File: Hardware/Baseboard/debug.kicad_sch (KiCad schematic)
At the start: 1 part, among them J1 Conn_02x06_Odd_Even

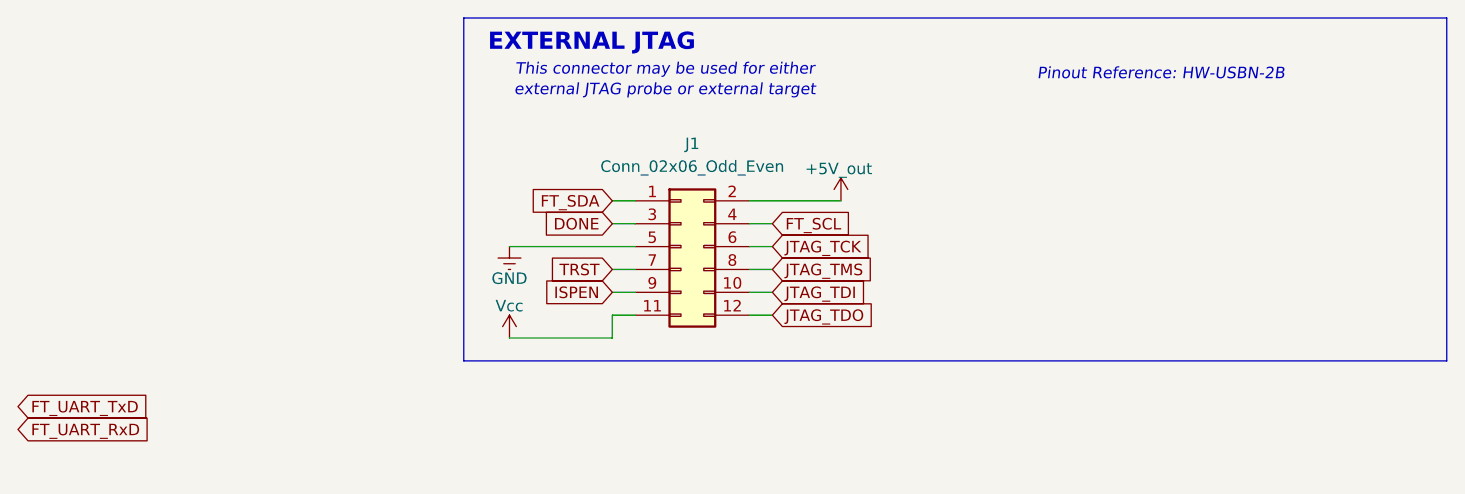
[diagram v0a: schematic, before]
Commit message: M.2 connector added
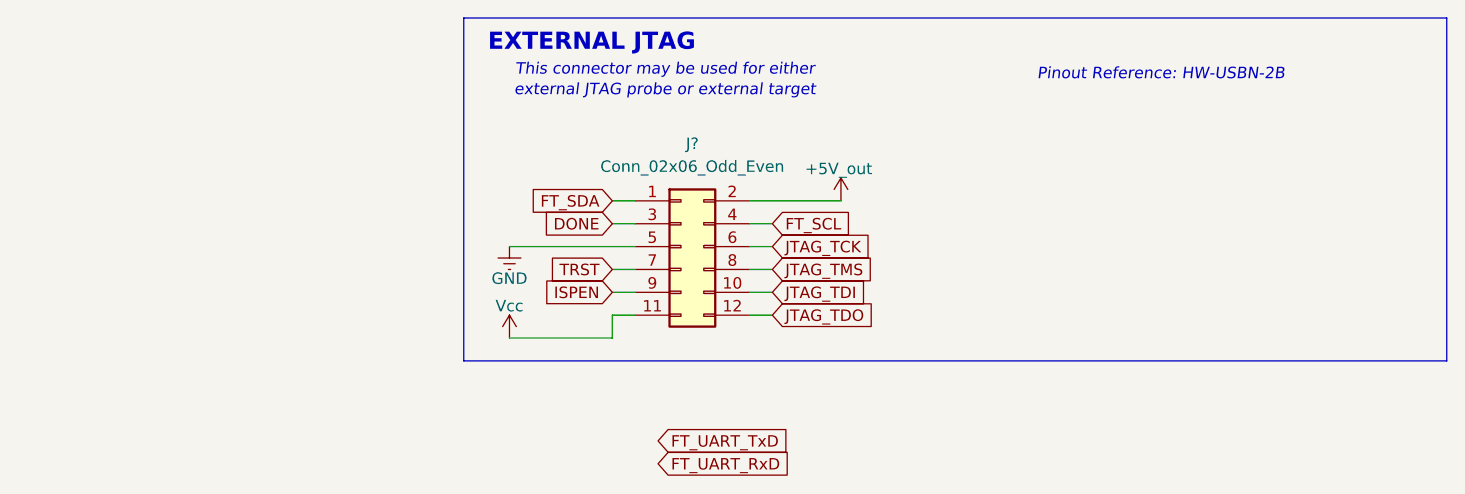
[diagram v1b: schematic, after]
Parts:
- renumbered J1 to J?
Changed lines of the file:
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@@
 	(global_label "FT_UART_RxD"
 		(shape input)
-		(at 71.12 72.39 0)
-		(fields_autoplaced yes)
-		(effects
-			(font
-				(size 1.27 1.27)
-			)
-			(justify left)
-		)
-		(property "Intersheetrefs" "${INTERSHEET_REFS}"
-			(at 86.3214 72.39 0)
+		(at 142.24 76.2 0)
+		(fields_autoplaced yes)
+		(effects
+			(font
+				(size 1.27 1.27)
+			)
+			(justify left)
+		)
+		(property "Intersheetrefs" "${INTERSHEET_REFS}"
+			(at 157.4414 76.2 0)
 			(effects
 				(font
@@
 	(global_label "FT_UART_TxD"
 		(shape input)
-		(at 71.12 69.85 0)
-		(fields_autoplaced yes)
-		(effects
-			(font
-				(size 1.27 1.27)
-			)
-			(justify left)
-		)
-		(property "Intersheetrefs" "${INTERSHEET_REFS}"
-			(at 86.019 69.85 0)
+		(at 142.24 73.66 0)
+		(fields_autoplaced yes)
+		(effects
+			(font
+				(size 1.27 1.27)
+			)
+			(justify left)
+		)
+		(property "Intersheetrefs" "${INTERSHEET_REFS}"
+			(at 157.139 73.66 0)
 			(effects
 				(font
@@
 		(dnp no)
 		(fields_autoplaced yes)
-		(property "Reference" "J1"
+		(property "Reference" "J?"
 			(at 146.05 40.64 0)
 			(effects
@@
 		)
 		(instances
-			(project ""
+			(project "FPGA4RISCV_BB"
 				(path "/de32abb0-ff3b-4c67-a91a-eed08140b1b2/70720321-4fb8-41e5-9369-c55119823db0"
-					(reference "J1")
+					(reference "J?")
 					(unit 1)
 				)

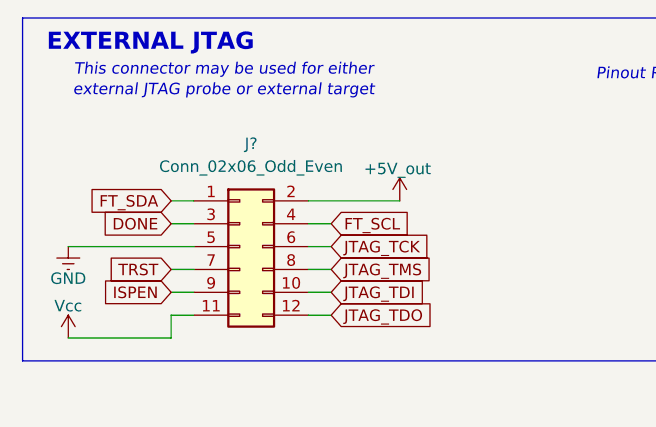
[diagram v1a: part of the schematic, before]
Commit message: PCIe M.2 connector changed
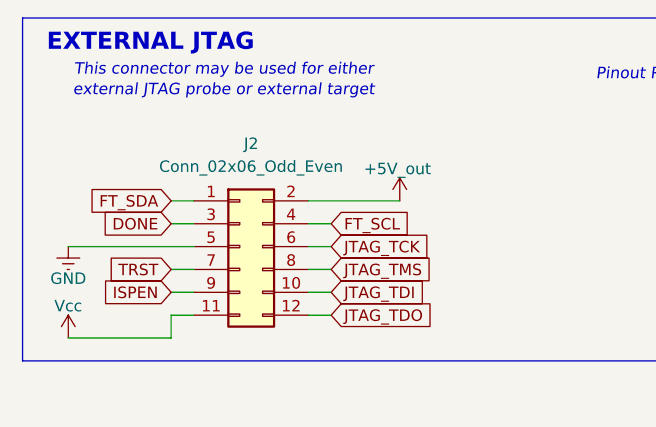
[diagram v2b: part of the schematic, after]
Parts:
- gave numbers to parts that had none: 1
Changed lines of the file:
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@@
 		(on_board yes)
 		(dnp no)
-		(property "Reference" "#PWR023"
+		(property "Reference" "#PWR02"
 			(at 125.73 66.04 0)
 			(effects
@@
 			(project "FPGA4RISCV_BB"
 				(path "/de32abb0-ff3b-4c67-a91a-eed08140b1b2/70720321-4fb8-41e5-9369-c55119823db0"
-					(reference "#PWR023")
+					(reference "#PWR02")
 					(unit 1)
 				)
@@
 		(on_board yes)
 		(dnp no)
-		(property "Reference" "#PWR022"
+		(property "Reference" "#PWR03"
 			(at 162.56 50.8 0)
 			(effects
@@
 			(project "FPGA4RISCV_BB"
 				(path "/de32abb0-ff3b-4c67-a91a-eed08140b1b2/70720321-4fb8-41e5-9369-c55119823db0"
-					(reference "#PWR022")
+					(reference "#PWR03")
 					(unit 1)
 				)
@@
 		(on_board yes)
 		(dnp no)
-		(property "Reference" "#PWR021"
+		(property "Reference" "#PWR01"
 			(at 125.73 58.42 0)
 			(effects
@@
 			(project "FPGA4RISCV_BB"
 				(path "/de32abb0-ff3b-4c67-a91a-eed08140b1b2/70720321-4fb8-41e5-9369-c55119823db0"
-					(reference "#PWR021")
+					(reference "#PWR01")
 					(unit 1)
 				)
@@
 		(dnp no)
 		(fields_autoplaced yes)
-		(property "Reference" "J?"
+		(property "Reference" "J2"
 			(at 146.05 40.64 0)
 			(effects
@@
 			(project "FPGA4RISCV_BB"
 				(path "/de32abb0-ff3b-4c67-a91a-eed08140b1b2/70720321-4fb8-41e5-9369-c55119823db0"
-					(reference "J?")
-					(unit 1)
-				)
+					(reference "J2")
+					(unit 1)
+				)
